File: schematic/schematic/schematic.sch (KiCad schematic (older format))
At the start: 103 parts

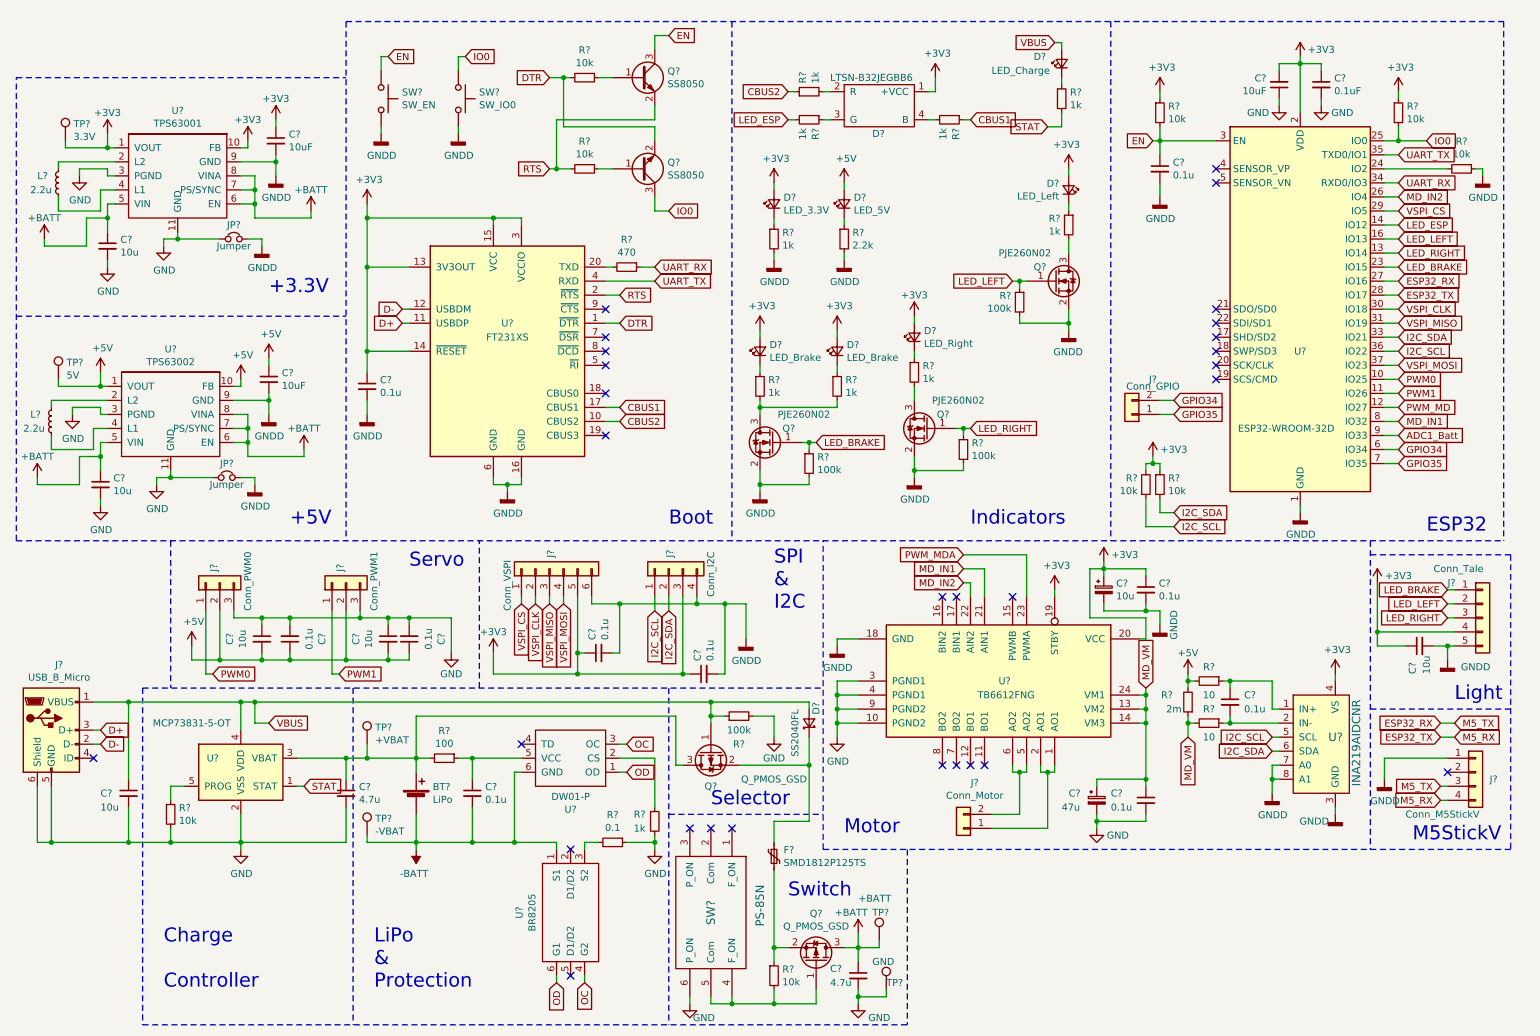
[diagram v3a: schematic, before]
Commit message: add USB-A port
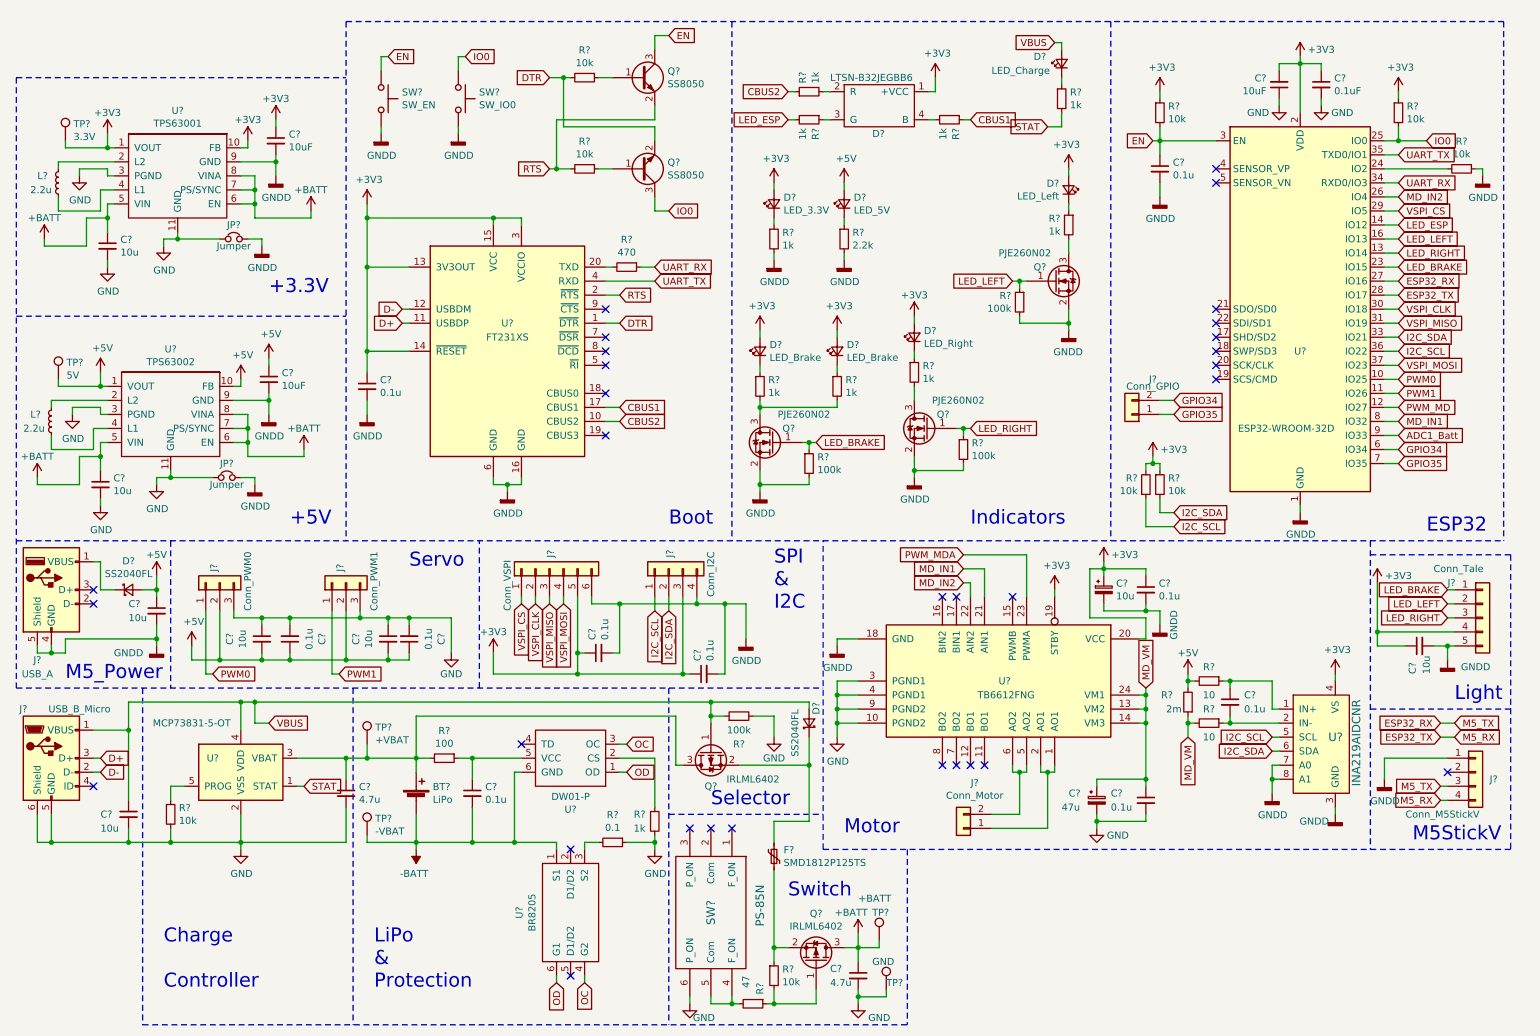
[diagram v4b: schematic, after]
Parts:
- added C?: 10u, symbol Device:C_Small
- added D?: SS2040FL, symbol Device:D_Schottky_Small
- added J?: USB_A, symbol Connector:USB_A
- added R?: 47, symbol Device:R_Small
- Q? (x2): value Q_PMOS_GSD -> IRLML6402
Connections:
- net +5V: now also C?.1, D?.2 (A)
- net GNDD: now also C?.2, J?.4 (GND), J?.5 (Shield)
- net at Q?.1 (G), R?.2: now also R?.1; no longer SW?.4 (F_ON), SW?.5 (Com)
- new net: D?.1 (K), J?.1 (VBUS)
- new net: R?.2, SW?.4 (F_ON), SW?.5 (Com)
- no-connect marks 29 -> 31
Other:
- note added: "M5_Power"
- moved on the sheet: C?, J?
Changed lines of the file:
@@
 P 6200 7300
 F 0 "Q?" V 6543 7300 50  0000 C CNN
-F 1 "Q_PMOS_GSD" V 6452 7300 50  0000 C CNN
+F 1 "IRLML6402" V 6452 7300 50  0000 C CNN
 F 2 "" H 6400 7400 50  0001 C CNN
 F 3 "~" H 6200 7300 50  0001 C CNN
@@
 L Connector:USB_B_Micro J?
 U 1 1 5E11F2BF
-P 750 5650
-F 0 "J?" H 805 6117 50  0000 C CNN
-F 1 "USB_B_Micro" H 805 6026 50  0000 C CNN
-F 2 "" H 900 5600 50  0001 C CNN
-F 3 "~" H 900 5600 50  0001 C CNN
-	1    750  5650
+P 750 5850
+F 0 "J?" H 550 6200 50  0000 C CNN
+F 1 "USB_B_Micro" H 950 6200 50  0000 C CNN
+F 2 "" H 900 5800 50  0001 C CNN
+F 3 "~" H 900 5800 50  0001 C CNN
+	1    750  5850
 	1    0    0    -1
 $EndComp
@@
 L Device:C_Small C?
 U 1 1 5E16D30E
-P 1300 6100
-F 0 "C?" H 1100 6100 50  0000 L CNN
-F 1 "10u" H 1100 6000 50  0000 L CNN
-F 2 "" H 1300 6100 50  0001 C CNN
-F 3 "~" H 1300 6100 50  0001 C CNN
-	1    1300 6100
+P 1300 6250
+F 0 "C?" H 1100 6250 50  0000 L CNN
+F 1 "10u" H 1100 6150 50  0000 L CNN
+F 2 "" H 1300 6250 50  0001 C CNN
+F 3 "~" H 1300 6250 50  0001 C CNN
+	1    1300 6250
 	1    0    0    -1
 $EndComp
 Wire Wire Line
-	1300 6200 1300 6450
-Wire Wire Line
 	3350 5850 3350 5950
 Wire Wire Line
@@
 Wire Wire Line
 	3350 6450 3350 6250
-Connection ~ 1300 6450
-Wire Wire Line
-	1300 6450 1600 6450
 $Comp
 L Device:Q_PMOS_GSD Q?
@@
 P 5450 5800
 F 0 "Q?" V 5700 5800 50  0000 C CNN
-F 1 "Q_PMOS_GSD" V 5650 5350 50  0000 C CNN
+F 1 "IRLML6402" V 5650 5500 50  0000 C CNN
 F 2 "" H 5650 5900 50  0001 C CNN
 F 3 "~" H 5450 5800 50  0001 C CNN
@@
 Wire Wire Line
 	2100 5450 2200 5450
-Wire Wire Line
-	1300 5450 1300 6000
 $Comp
 L Device:R_Small R?
@@
 NoConn ~ 4450 7400
 NoConn ~ 4100 5750
-Connection ~ 1300 5450
 Connection ~ 2100 5450
 Wire Wire Line
@@
 	500  2700 2850 2700
 Wire Notes Line
-	500  4300 500  1000
-Wire Notes Line
 	500  1000 2850 1000
 Text Notes 2300 2550 0    100  ~ 0
@@
 	1    0    0    -1
 $EndComp
-Wire Notes Line
-	1400 5350 6250 5350
 Wire Wire Line
 	5200 5900 5200 5550
@@
 	1    0    0    -1
 $EndComp
-NoConn ~ 1050 5850
-Wire Wire Line
-	650  6050 650  6450
-Wire Wire Line
-	650  6450 750  6450
+NoConn ~ 1050 6050
 Wire Wire Line
-	750  6050 750  6450
-Connection ~ 750  6450
-Wire Wire Line
-	750  6450 1300 6450
-Wire Wire Line
-	1050 5450 1300 5450
-Wire Wire Line
-	1050 5650 1100 5650
-Text GLabel 1100 5650 2    50   Input ~ 0
+	1050 5850 1100 5850
+Text GLabel 1100 5850 2    50   Input ~ 0
 D+
-Text GLabel 1100 5750 2    50   Input ~ 0
+Text GLabel 1100 5950 2    50   Input ~ 0
 D-
 Wire Wire Line
-	1100 5750 1050 5750
+	1100 5950 1050 5950
 $Comp
 L Device:Q_NPN_BEC Q?
@@
 Wire Wire Line
 	5600 7600 5600 7550
-Connection ~ 5600 7600
-Connection ~ 5900 7600
 Wire Wire Line
 	6500 7200 6500 7300
@@
 	5150 5350 5150 7750
 Wire Wire Line
-	5600 7600 5900 7600
-Wire Wire Line
 	6500 7500 6500 7550
 Wire Wire Line
@@
 Wire Wire Line
 	8550 5600 8550 6000
+Wire Wire Line
+	650  6450 750  6450
+Wire Wire Line
+	1300 6350 1300 6450
+Connection ~ 1300 6450
+Wire Wire Line
+	1300 6450 1600 6450
+Wire Wire Line
+	650  6250 650  6450
+Wire Wire Line
+	750  6250 750  6450
+Connection ~ 750  6450
+Wire Wire Line
+	750  6450 1300 6450
+Wire Wire Line
+	1300 5450 1300 5650
+Wire Wire Line
+	1050 5650 1300 5650
+Connection ~ 1300 5650
+Wire Wire Line
+	1300 5650 1300 6150
+Wire Notes Line
+	500  1000 500  5350
+Wire Notes Line
+	500  5350 6250 5350
+$Comp
+L Connector:USB_A J?
+U 1 1 5E2ED068
+P 750 4650
+F 0 "J?" H 650 4150 50  0000 C CNN
+F 1 "USB_A" H 650 4050 50  0000 C CNN
+F 2 "" H 900 4600 50  0001 C CNN
+F 3 " ~" H 900 4600 50  0001 C CNN
+	1    750  4650
+	1    0    0    -1
+$EndComp
+$Comp
+L power:+5V #PWR?
+U 1 1 5E39788C
+P 1500 4550
+F 0 "#PWR?" H 1500 4400 50  0001 C CNN
+F 1 "+5V" H 1500 4700 50  0000 C CNN
+F 2 "" H 1500 4550 50  0001 C CNN
+F 3 "" H 1500 4550 50  0001 C CNN
+	1    1500 4550
+	1    0    0    -1
+$EndComp
+NoConn ~ 1050 4650
+NoConn ~ 1050 4750
+Wire Wire Line
+	650  5050 650  5100
+Wire Wire Line
+	750  5100 750  5050
+$Comp
+L power:GNDD #PWR?
+U 1 1 5E47D949
+P 1500 5050
+F 0 "#PWR?" H 1500 4800 50  0001 C CNN
+F 1 "GNDD" H 1300 5000 50  0000 C CNN
+F 2 "" H 1500 5050 50  0001 C CNN
+F 3 "" H 1500 5050 50  0001 C CNN
+	1    1500 5050
+	1    0    0    -1
+$EndComp
+Wire Wire Line
+	650  5100 750  5100
+Wire Wire Line
+	750  5100 850  5100
+Wire Wire Line
+	850  5100 850  5000
+Connection ~ 750  5100
+Text Notes 850  5300 0    100  ~ 0
+M5_Power
+Wire Wire Line
+	1100 4450 1050 4450
+$Comp
+L Device:C_Small C?
+U 1 1 5E5E4FAC
+P 1500 4800
+F 0 "C?" H 1300 4850 50  0000 L CNN
+F 1 "10u" H 1300 4750 50  0000 L CNN
+F 2 "" H 1500 4800 50  0001 C CNN
+F 3 "~" H 1500 4800 50  0001 C CNN
+	1    1500 4800
+	1    0    0    -1
+$EndComp
+Wire Wire Line
+	1500 4900 1500 5000
+Wire Wire Line
+	1500 5000 1500 5050
+Connection ~ 1500 5000
+Wire Wire Line
+	1100 4450 1100 4650
+Wire Wire Line
+	850  5000 1500 5000
+Wire Wire Line
+	1100 4650 1200 4650
+Wire Wire Line
+	1400 4650 1500 4650
+Connection ~ 1500 4650
+Wire Wire Line
+	1500 4650 1500 4700
+Wire Wire Line
+	1500 4550 1500 4650
+$Comp
+L Device:D_Schottky_Small D?
+U 1 1 5E841DFC
+P 1300 4650
+F 0 "D?" H 1300 4855 50  0000 C CNN
+F 1 "SS2040FL" H 1300 4764 50  0000 C CNN
+F 2 "" V 1300 4650 50  0001 C CNN
+F 3 "~" V 1300 4650 50  0001 C CNN
+	1    1300 4650
+	1    0    0    -1
+$EndComp
+$Comp
+L Device:R_Small R?
+U 1 1 5E93AE39
+P 5750 7600
+F 0 "R?" H 5600 7650 50  0000 L CNN
+F 1 "47" H 5550 7550 50  0000 L CNN
+F 2 "" H 5750 7600 50  0001 C CNN
+F 3 "~" H 5750 7600 50  0001 C CNN
+	1    5750 7600
+	0    1    1    0
+$EndComp
+Wire Wire Line
+	5650 7600 5600 7600
+Connection ~ 5600 7600
+Wire Wire Line
+	5850 7600 5900 7600
+Connection ~ 5900 7600
 $EndSCHEMATC

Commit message: remove ESP_LED
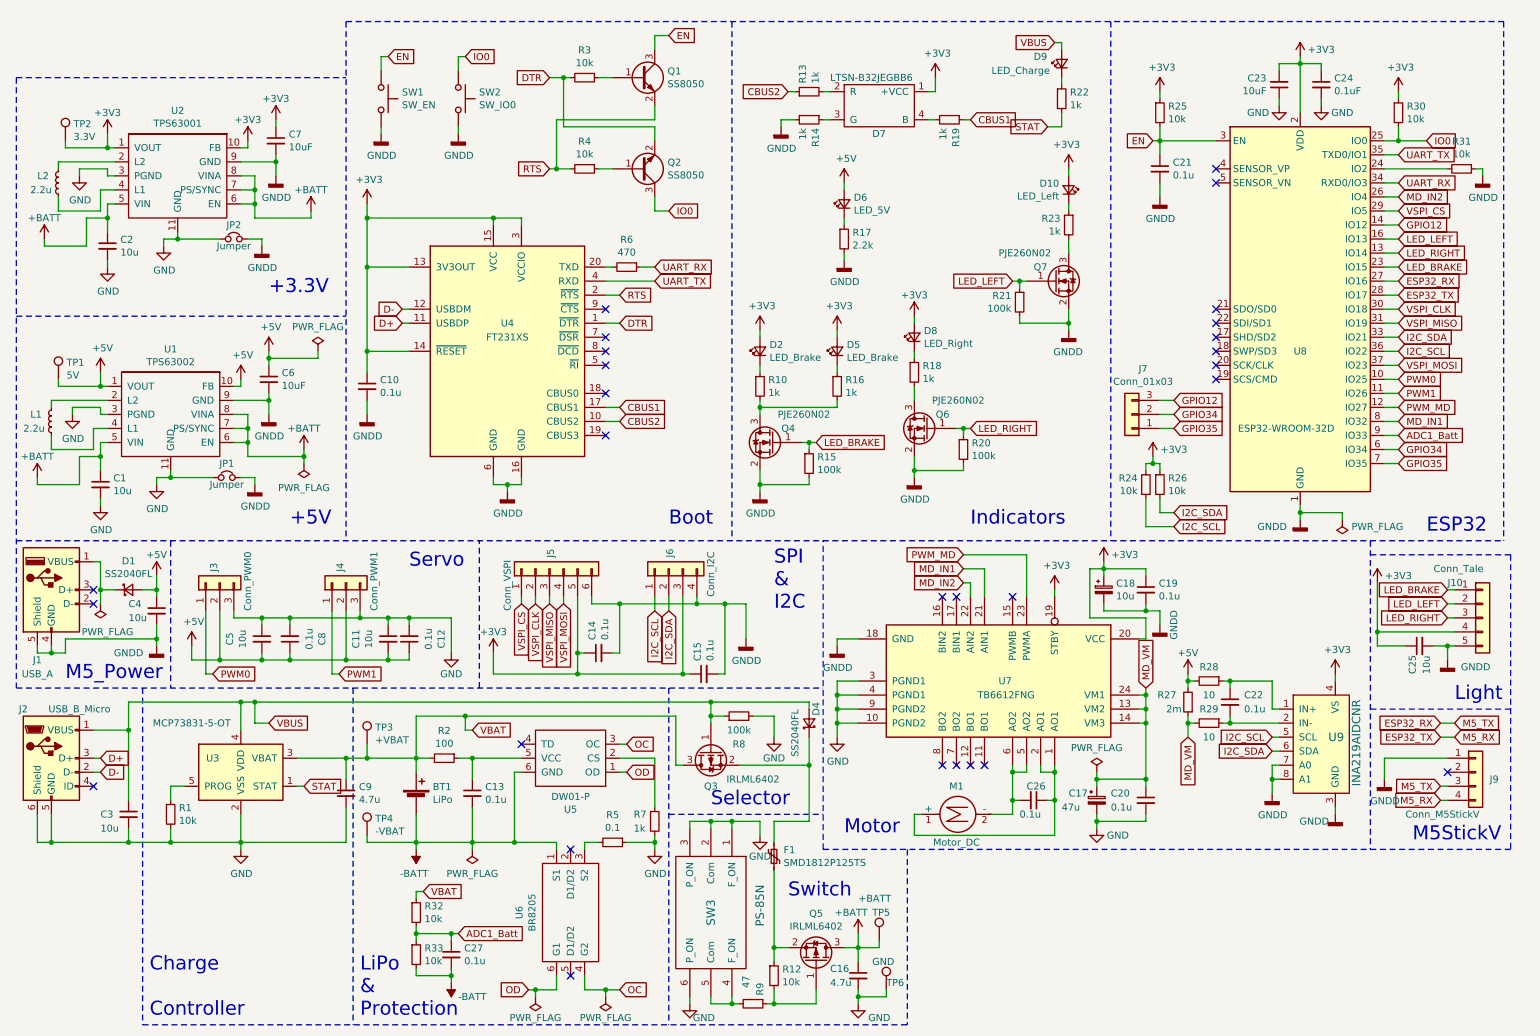
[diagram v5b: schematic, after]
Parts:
- removed D?: LED_3.3V, symbol Device:LED_Small
- removed J?: Conn_Motor, symbol Connector_Generic:Conn_01x02
- removed J?: Conn_GPIO, symbol Connector_Generic:Conn_01x02
- removed R?: 1k, symbol Device:R_Small
- added C26, C27: 0.1u, symbol Device:C_Small
- added J7: Conn_01x03, symbol Connector_Generic:Conn_01x03
- added M1: Motor_DC, symbol Motor:Motor_DC
- added R32, R33: 10k, symbol Device:R_Small
- gave numbers to parts that had none: 103
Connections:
- net PWM_MDA is gone; now on net PWM_MD: U7.23 (PWMA)
- net -BATT: now also C27.2, R33.2
- net ADC1_Batt: now also C27.1, R32.2, R33.1
- net GND: now also SW3.1 (F_ON), SW3.2 (Com), SW3.3 (P_ON)
- net GNDD: now also R14.2
- net GPIO34: now also J7.2 (Pin_2)
- net GPIO35: now also J7.1 (Pin_1)
- net VBAT: now reaches BT1.1 (+), C9.1, Q3.3 (D), R2.2, TP3.1, U3.3 (VBAT)
- net VBAT: now also R32.1
- net at U7.1 (AO1), U7.2 (AO1): now also C26.1, M1.1 (+)
- net at U7.5 (AO2), U7.6 (AO2): now also C26.2, M1.2 (-)
- net LED_ESP renamed GPIO12
- net GPIO12: now also J7.3 (Pin_3); no longer R14.2
- no-connect marks 31 -> 28

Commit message: Accelometer Test has done
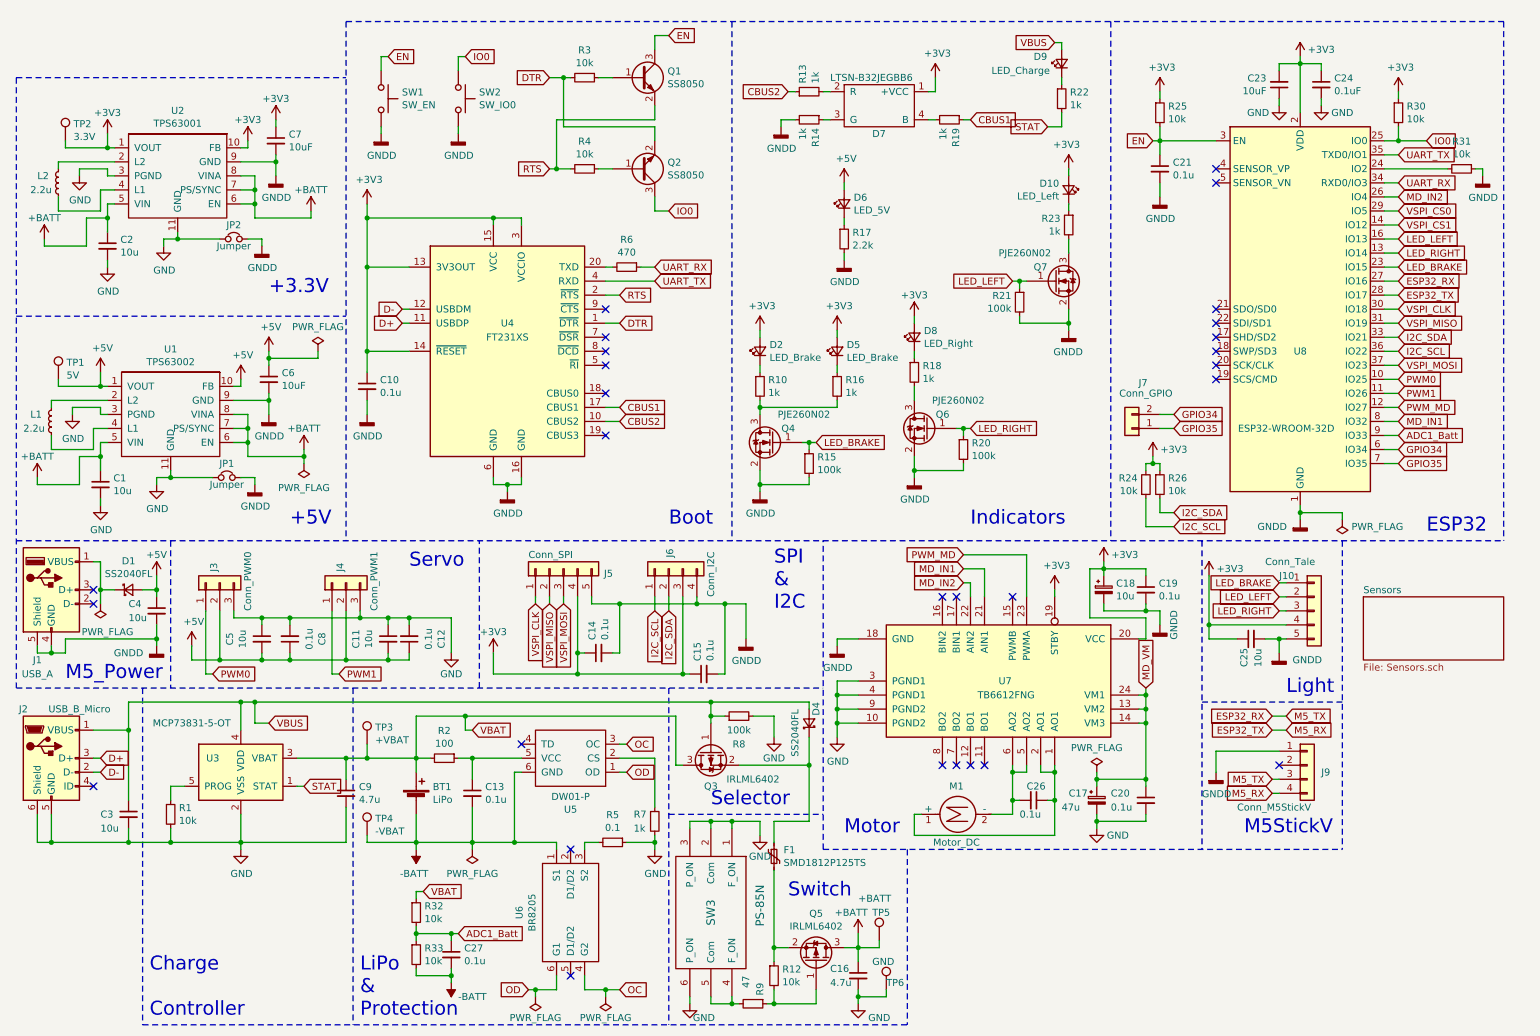
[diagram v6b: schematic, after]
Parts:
- removed C22: 0.1u, symbol Device:C_Small
- removed J5: Conn_VSPI, symbol Connector_Generic:Conn_01x06
- removed J7: Conn_01x03, symbol Connector_Generic:Conn_01x03
- removed R27: 2m, symbol Device:R_Small
- removed R28, R29: 10, symbol Device:R_Small
- removed U9: INA219AIDCNR, digikey-footprints:SOT-23-8, symbol dk_PMIC-Current-Regulation-Management:INA219AIDCNR
- added J5: Conn_SPI, symbol Connector_Generic:Conn_01x05
- added J7: Conn_GPIO, symbol Connector_Generic:Conn_01x02
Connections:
- net +3V3: now also J5.4 (Pin_4)
- net GNDD: now also J5.5 (Pin_5)
- net GPIO34: now also J7.2 (Pin_2)
- net GPIO35: now also J7.1 (Pin_1)
- net VSPI_CLK: now also J5.1 (Pin_1)
- net VSPI_MISO: now also J5.2 (Pin_2)
- net VSPI_MOSI: now also J5.3 (Pin_3)
- net GPIO12 renamed VSPI_CS1
- net VSPI_CS renamed VSPI_CS0
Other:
- moved on the sheet: C25, J10, J9

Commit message: assign footprint
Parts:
- added J8: Conn_Tale, symbol Connector_Generic:Conn_01x05
- BT1: footprint (none) -> Connector_JST:JST_PH_B2B-PH-K_1x02_P2.00mm_Vertical
- C1, C11, C18, C2, C25, C3, C4, C5: footprint (none) -> Capacitor_SMD:C_0603_1608Metric_Pad1.05x0.95mm_HandSolder
- C10, C12, C13, C14, C15, C16, C19, C20, C21, C26, C27, C8, C9: footprint (none) -> micelib:C_0402_1005Metric_HandSoldering
- C17: footprint (none) -> Capacitor_SMD:C_1210_3225Metric_Pad1.42x2.65mm_HandSolder
- C23, C6, C7: value 10uF -> 10u; footprint (none) -> Capacitor_SMD:C_0603_1608Metric_Pad1.05x0.95mm_HandSolder
- C24: value 0.1uF -> 0.1u; footprint (none) -> micelib:C_0402_1005Metric_HandSoldering
- L1, L2: footprint (none) -> micelib:SPM3015-xRxM-LR
- M1: footprint (none) -> Connector_PinHeader_2.54mm:PinHeader_1x02_P2.54mm_Vertical
- TP1, TP2, TP3, TP4, TP5, TP6: footprint (none) -> Connector_PinHeader_1.27mm:PinHeader_1x01_P1.27mm_Vertical
- U1, U2: footprint (none) -> micelib:WSON-10-1EP_2x3mm_P0.5mm_EP0.84x2.4mm_TPS6300x
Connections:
- net +3V3: now also J8.4 (Pin_4)
- net GNDD: now also J8.5 (Pin_5)
- net LED_BRAKE: now also J8.1 (Pin_1)
- net LED_LEFT: now also J8.2 (Pin_2)
- net LED_RIGHT: now also J8.3 (Pin_3)
